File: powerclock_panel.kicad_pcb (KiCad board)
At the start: 2 copper layers, 30 x 128.5 mm, 1 part

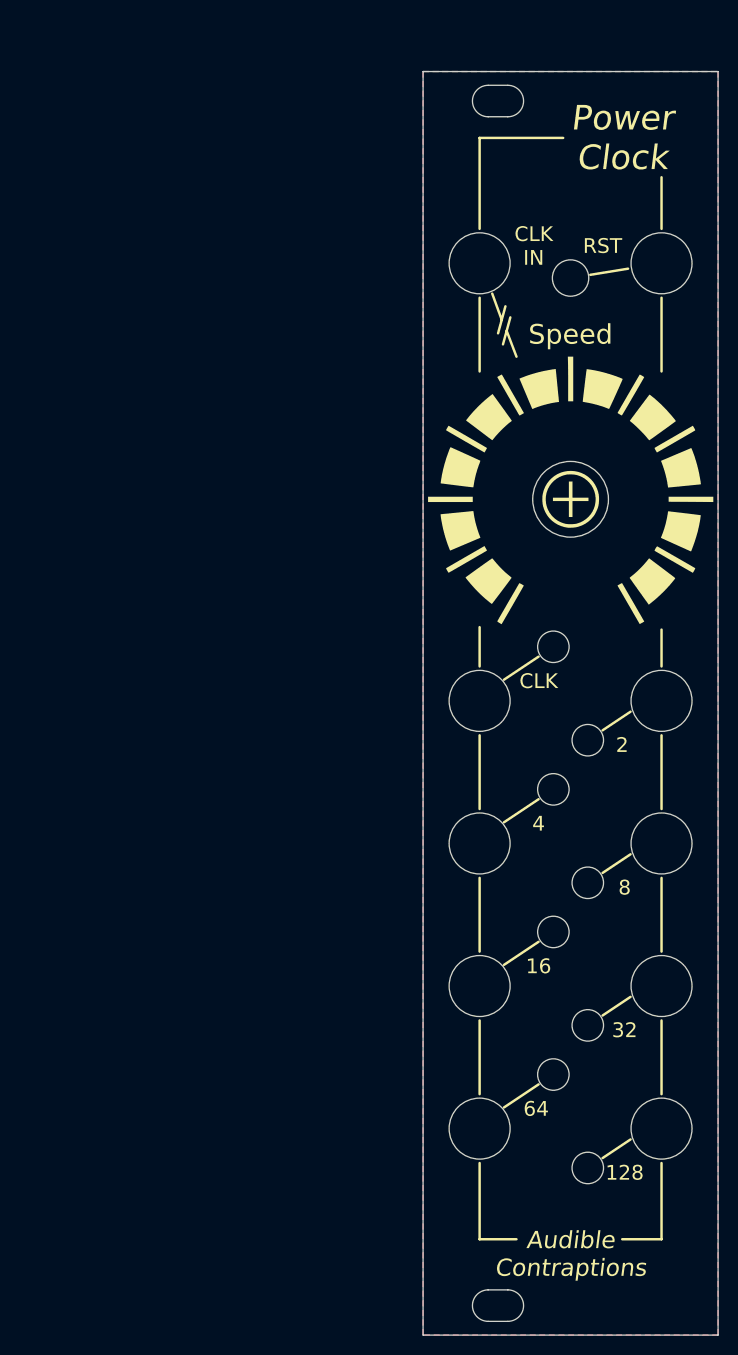
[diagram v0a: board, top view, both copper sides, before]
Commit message: Add license disclaimers
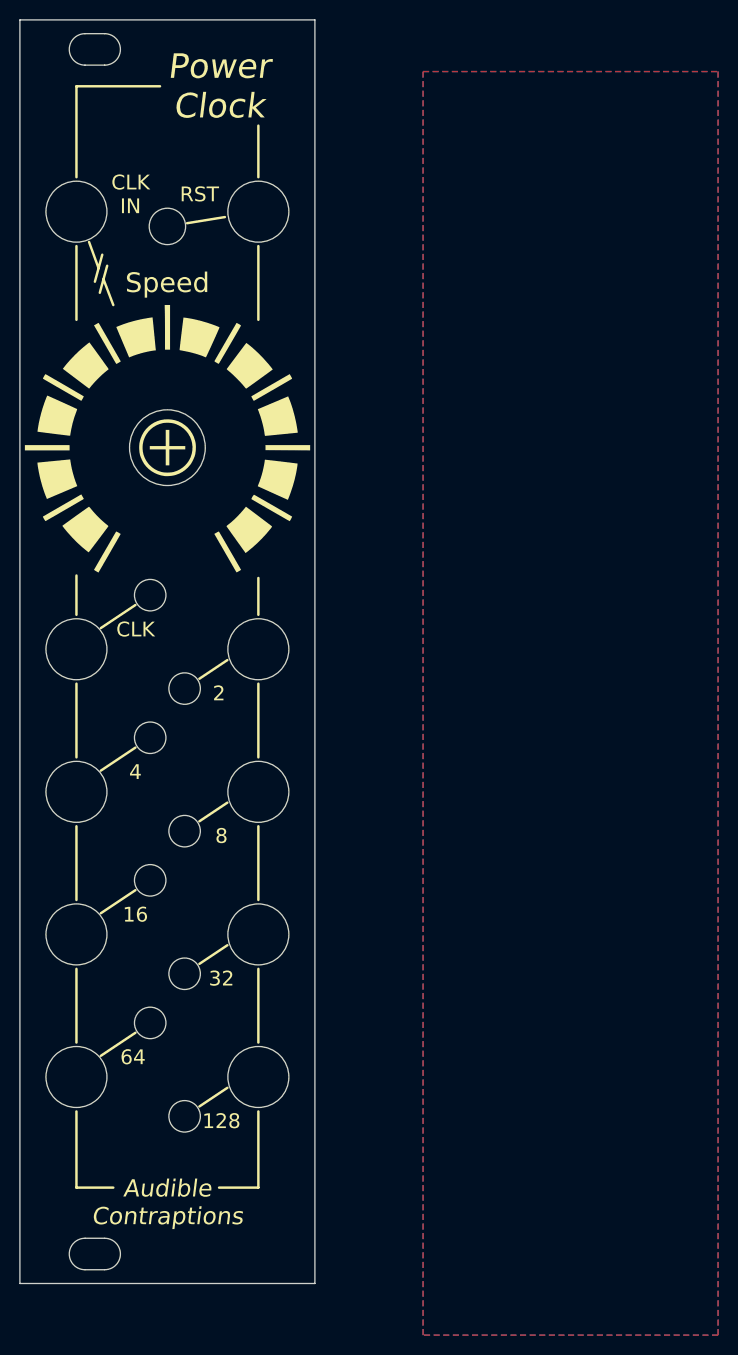
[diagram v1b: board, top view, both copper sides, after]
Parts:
- moved G*** 41.3 mm to (74.0, 68.2)
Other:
- board text added: "rev2_20230306ab"
- board text removed: "JLCJLCJLCJLC"
- board text removed: "v1 20230217"
